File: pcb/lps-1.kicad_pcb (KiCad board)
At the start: 4 copper layers, 66.2 x 30 mm, 26 parts, among them J15 PWR, J4 A_INA219, J5 XBEE, J6 DEV, U1 L7805, U2 ATMega1608_32, U3 TC1262-33

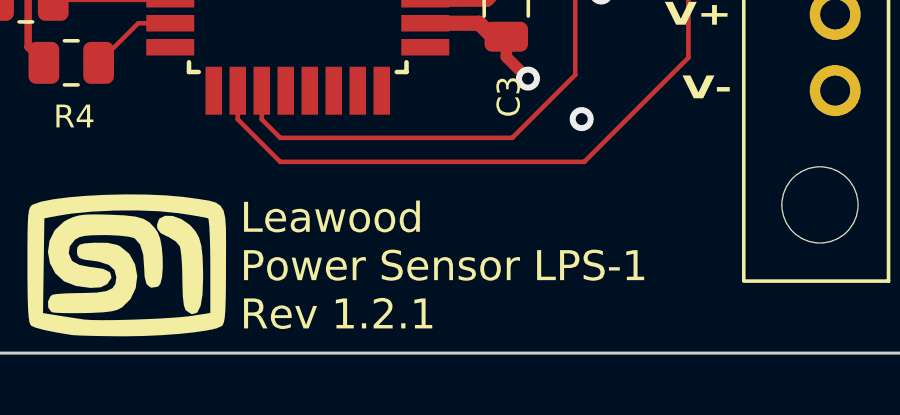
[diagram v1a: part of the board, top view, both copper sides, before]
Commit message: Adds release script
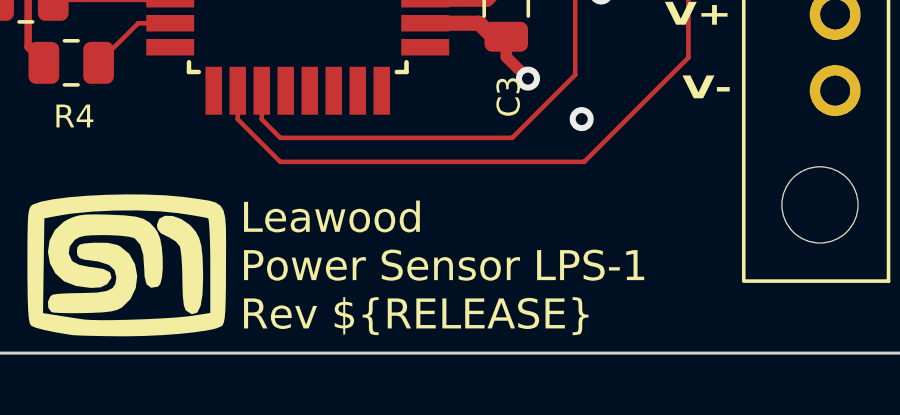
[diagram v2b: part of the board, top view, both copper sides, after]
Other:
- board text added: "Leawood Power Sensor LPS-1 Rev ${REVISION}"
